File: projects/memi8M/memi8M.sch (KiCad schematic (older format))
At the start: 38 parts, among them J1 Conn_01x06, J2 Conn_01x02, J3 Conn_01x03, J4 Conn_01x06, SW1 SW_DIP_x05, U1 74HC595N, U10 74LS166N, U11 SST39VF1681_1682, U12 74LVC4245, U2 74HC595N, U3 74HC595N, U4 74HC595N, U5 SFC_MaskRom_32pin_SOCKET, U6 74LVC245, U7 74LVC245, U8 74LVC245, U9 LD1117S33TR

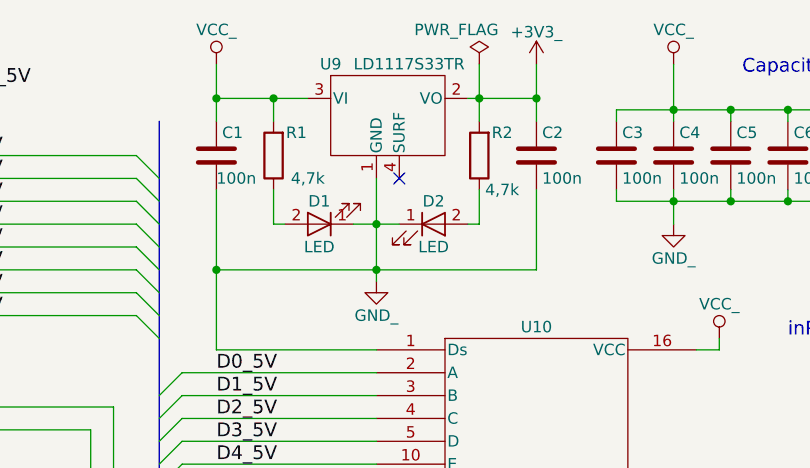
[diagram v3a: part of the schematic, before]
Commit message: Some module renamed for better overall accessibility. BOM updated. .net created. Modules associated to .net and schema.
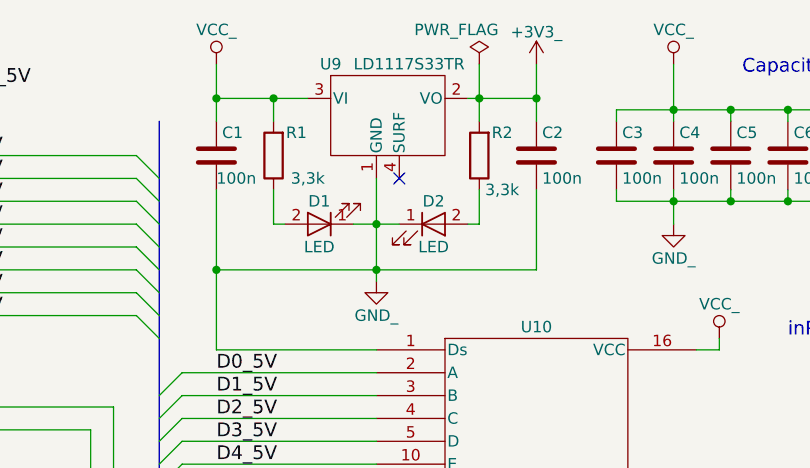
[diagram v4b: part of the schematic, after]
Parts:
- C1, C10, C11, C12, C13, C2, C3, C4, C5, C6, C7, C8, C9, D1, D2, R3, R4, R5, R6: footprint (none) -> alf64_mods:0805
- J1, J4: footprint PINHEAD1x6 -> alf64_mods:PINHEAD1x6
- J2: footprint PINHEAD1x2 -> alf64_mods:PINHEAD1x2
- J3: footprint PINHEAD1x3 -> alf64_mods:PINHEAD1x3
- R1, R2: value 4,7k -> 3,3k; footprint (none) -> alf64_mods:0805
- SW1: footprint (none) -> alf64_mods:SW_DIP_x05
- U1, U2, U3, U4: footprint SO16 -> alf64_mods:SO16
- U10: footprint (none) -> alf64_mods:SO16
- U11: footprint (none) -> alf64_mods:GOTRONIK_ADAP_TSOP48
- U12: footprint (none) -> alf64_mods:SO24
- U5: footprint PDIP32 -> alf64_mods:PDIP32
- U6, U7, U8: footprint 74LVC245_SO20 -> alf64_mods:SO20
- U9: footprint (none) -> alf64_mods:SOT223
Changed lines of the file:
@@
 F 0 "U1" H 2050 1900 50  0000 C CNN
 F 1 "74HC595N" H 1900 700 50  0000 C CNN
-F 2 "SO16" H 1900 1300 50  0001 C CNN
+F 2 "alf64_mods:SO16" H 1900 1300 50  0001 C CNN
 F 3 "" H 1900 1300 50  0001 C CNN
 	1    1900 1300
@@
 F 0 "U2" H 2050 3300 50  0000 C CNN
 F 1 "74HC595N" H 1900 2100 50  0000 C CNN
-F 2 "SO16" H 1900 2700 50  0001 C CNN
+F 2 "alf64_mods:SO16" H 1900 2700 50  0001 C CNN
 F 3 "" H 1900 2700 50  0001 C CNN
 	1    1900 2700
@@
 F 0 "U3" H 2050 4700 50  0000 C CNN
 F 1 "74HC595N" H 1900 3500 50  0000 C CNN
-F 2 "SO16" H 1900 4100 50  0001 C CNN
+F 2 "alf64_mods:SO16" H 1900 4100 50  0001 C CNN
 F 3 "" H 1900 4100 50  0001 C CNN
 	1    1900 4100
@@
 F 0 "U6" H 4700 4600 60  0000 C CNN
 F 1 "74LVC245" H 4700 3400 60  0000 C CNN
-F 2 "74LVC245_SO20" H 4700 3300 60  0001 C CNN
+F 2 "alf64_mods:SO20" H 4700 3300 60  0001 C CNN
 F 3 "" H 4700 4000 60  0001 C CNN
 	1    4700 4000
@@
 F 0 "U7" H 4700 6050 60  0000 C CNN
 F 1 "74LVC245" H 4700 4850 60  0000 C CNN
-F 2 "74LVC245_SO20" H 4700 4750 60  0001 C CNN
+F 2 "alf64_mods:SO20" H 4700 4750 60  0001 C CNN
 F 3 "" H 4700 5450 60  0001 C CNN
 	1    4700 5450
@@
 F 0 "U8" H 4700 7500 60  0000 C CNN
 F 1 "74LVC245" H 4700 6300 60  0000 C CNN
-F 2 "74LVC245_SO20" H 4700 6200 60  0001 C CNN
+F 2 "alf64_mods:SO20" H 4700 6200 60  0001 C CNN
 F 3 "" H 4700 6900 60  0001 C CNN
 	1    4700 6900
@@
 F 0 "U5" H 4750 2450 60  0000 C CNN
 F 1 "SFC_MaskRom_32pin_SOCKET" H 4700 200 60  0000 C CNN
-F 2 "PDIP32" H 4750 2450 60  0001 C CNN
+F 2 "alf64_mods:PDIP32" H 4750 2450 60  0001 C CNN
 F 3 "" H 4750 2450 60  0001 C CNN
 	1    4750 1550
@@
 F 0 "U11" H 7250 5400 60  0000 C CNN
 F 1 "SST39VF1681_1682" H 7250 3150 60  0000 C CNN
-F 2 "" H 7250 5400 60  0001 C CNN
+F 2 "alf64_mods:GOTRONIK_ADAP_TSOP48" H 7250 5400 60  0001 C CNN
 F 3 "" H 7250 5400 60  0001 C CNN
 	1    7250 4600
@@
 F 0 "U4" H 2050 6100 50  0000 C CNN
 F 1 "74HC595N" H 1900 4900 50  0000 C CNN
-F 2 "SO16" H 1900 5500 50  0001 C CNN
+F 2 "alf64_mods:SO16" H 1900 5500 50  0001 C CNN
 F 3 "" H 1900 5500 50  0001 C CNN
 	1    1900 5500
@@
 F 0 "U12" H 9000 5000 60  0000 C CNN
 F 1 "74LVC4245" H 9000 3600 60  0000 C CNN
-F 2 "" H 9000 4400 60  0001 C CNN
+F 2 "alf64_mods:SO24" H 9000 4400 60  0001 C CNN
 F 3 "" H 9000 4400 60  0001 C CNN
 	1    9000 4400
@@
 F 0 "U10" H 8100 3400 50  0000 C CNN
 F 1 "74LS166N" H 8100 1900 50  0000 C CNN
-F 2 "" H 8100 2650 50  0001 C CNN
+F 2 "alf64_mods:SO16" H 8100 2650 50  0001 C CNN
 F 3 "" H 8100 2650 50  0001 C CNN
 	1    8100 2650
@@
 F 0 "C1" H 6725 1250 50  0000 L CNN
 F 1 "100n" H 6700 1050 50  0000 L CNN
-F 2 "" H 6738 1000 50  0001 C CNN
+F 2 "alf64_mods:0805" H 6738 1000 50  0001 C CNN
 F 3 "" H 6700 1150 50  0001 C CNN
 	1    6700 1150
@@
 F 0 "C2" H 8125 1250 50  0000 L CNN
 F 1 "100n" H 8125 1050 50  0000 L CNN
-F 2 "" H 8138 1000 50  0001 C CNN
+F 2 "alf64_mods:0805" H 8138 1000 50  0001 C CNN
 F 3 "" H 8100 1150 50  0001 C CNN
 	1    8100 1150
@@
 F 0 "R3" V 10750 1950 50  0000 C CNN
 F 1 "100" V 10800 2150 50  0000 C CNN
-F 2 "" V 10730 2150 50  0001 C CNN
+F 2 "alf64_mods:0805" V 10730 2150 50  0001 C CNN
 F 3 "" H 10800 2150 50  0001 C CNN
 	1    10800 2150
@@
 F 0 "R5" V 10750 2150 50  0000 C CNN
 F 1 "100" V 10800 2350 50  0000 C CNN
-F 2 "" V 10730 2350 50  0001 C CNN
+F 2 "alf64_mods:0805" V 10730 2350 50  0001 C CNN
 F 3 "" H 10800 2350 50  0001 C CNN
 	1    10800 2350
@@
 F 0 "R4" V 10750 2050 50  0000 C CNN
 F 1 "100" V 10800 2250 50  0000 C CNN
-F 2 "" V 10730 2250 50  0001 C CNN
+F 2 "alf64_mods:0805" V 10730 2250 50  0001 C CNN
 F 3 "" H 10800 2250 50  0001 C CNN
 	1    10800 2250
@@
 F 0 "J1" H 800 7050 50  0000 C CNN
 F 1 "Conn_01x06" H 800 6350 50  0000 C CNN
-F 2 "PINHEAD1x6" H 800 6750 50  0001 C CNN
+F 2 "alf64_mods:PINHEAD1x6" H 800 6750 50  0001 C CNN
 F 3 "" H 800 6750 50  0001 C CNN
 	1    800  6750
@@
 F 0 "J2" H 800 7550 50  0000 C CNN
 F 1 "Conn_01x02" H 800 7250 50  0000 C CNN
-F 2 "PINHEAD1x2" H 800 7450 50  0001 C CNN
+F 2 "alf64_mods:PINHEAD1x2" H 800 7450 50  0001 C CNN
 F 3 "" H 800 7450 50  0001 C CNN
 	1    800  7450
@@
 F 0 "J3" H 2800 6700 50  0000 C CNN
 F 1 "Conn_01x03" H 2800 6300 50  0000 C CNN
-F 2 "PINHEAD1x3" H 2800 6500 50  0001 C CNN
+F 2 "alf64_mods:PINHEAD1x3" H 2800 6500 50  0001 C CNN
 F 3 "" H 2800 6500 50  0001 C CNN
 	1    2800 6500
@@
 F 0 "R6" V 10750 2250 50  0000 C CNN
 F 1 "100" V 10800 2450 50  0000 C CNN
-F 2 "" V 10730 2450 50  0001 C CNN
+F 2 "alf64_mods:0805" V 10730 2450 50  0001 C CNN
 F 3 "" H 10800 2450 50  0001 C CNN
 	1    10800 2450
@@
 F 0 "C8" H 9725 1250 50  0000 L CNN
 F 1 "100n" H 9725 1050 50  0000 L CNN
-F 2 "" H 9738 1000 50  0001 C CNN
+F 2 "alf64_mods:0805" H 9738 1000 50  0001 C CNN
 F 3 "" H 9700 1150 50  0001 C CNN
 	1    9700 1150
@@
 F 0 "C10" H 10275 1250 50  0000 L CNN
 F 1 "100n" H 10275 1050 50  0000 L CNN
-F 2 "" H 10288 1000 50  0001 C CNN
+F 2 "alf64_mods:0805" H 10288 1000 50  0001 C CNN
 F 3 "" H 10250 1150 50  0001 C CNN
 	1    10250 1150
@@
 F 0 "C11" H 10525 1250 50  0000 L CNN
 F 1 "100n" H 10525 1050 50  0000 L CNN
-F 2 "" H 10538 1000 50  0001 C CNN
+F 2 "alf64_mods:0805" H 10538 1000 50  0001 C CNN
 F 3 "" H 10500 1150 50  0001 C CNN
 	1    10500 1150
@@
 F 0 "C12" H 10775 1250 50  0000 L CNN
 F 1 "100n" H 10775 1050 50  0000 L CNN
-F 2 "" H 10788 1000 50  0001 C CNN
+F 2 "alf64_mods:0805" H 10788 1000 50  0001 C CNN
 F 3 "" H 10750 1150 50  0001 C CNN
 	1    10750 1150
@@
 F 0 "C13" H 11025 1250 50  0000 L CNN
 F 1 "100n" H 11025 1050 50  0000 L CNN
-F 2 "" H 11038 1000 50  0001 C CNN
+F 2 "alf64_mods:0805" H 11038 1000 50  0001 C CNN
 F 3 "" H 11000 1150 50  0001 C CNN
 	1    11000 1150
@@
 F 0 "C3" H 8475 1250 50  0000 L CNN
 F 1 "100n" H 8475 1050 50  0000 L CNN
-F 2 "" H 8488 1000 50  0001 C CNN
+F 2 "alf64_mods:0805" H 8488 1000 50  0001 C CNN
 F 3 "" H 8450 1150 50  0001 C CNN
 	1    8450 1150
@@
 F 0 "C4" H 8725 1250 50  0000 L CNN
 F 1 "100n" H 8725 1050 50  0000 L CNN
-F 2 "" H 8738 1000 50  0001 C CNN
+F 2 "alf64_mods:0805" H 8738 1000 50  0001 C CNN
 F 3 "" H 8700 1150 50  0001 C CNN
 	1    8700 1150
@@
 F 0 "C5" H 8975 1250 50  0000 L CNN
 F 1 "100n" H 8975 1050 50  0000 L CNN
-F 2 "" H 8988 1000 50  0001 C CNN
+F 2 "alf64_mods:0805" H 8988 1000 50  0001 C CNN
 F 3 "" H 8950 1150 50  0001 C CNN
 	1    8950 1150
@@
 F 0 "C6" H 9225 1250 50  0000 L CNN
 F 1 "100n" H 9225 1050 50  0000 L CNN
-F 2 "" H 9238 1000 50  0001 C CNN
+F 2 "alf64_mods:0805" H 9238 1000 50  0001 C CNN
 F 3 "" H 9200 1150 50  0001 C CNN
 	1    9200 1150
@@
 F 0 "C7" H 9475 1250 50  0000 L CNN
 F 1 "100n" H 9475 1050 50  0000 L CNN
-F 2 "" H 9488 1000 50  0001 C CNN
+F 2 "alf64_mods:0805" H 9488 1000 50  0001 C CNN
 F 3 "" H 9450 1150 50  0001 C CNN
 	1    9450 1150
@@
 F 0 "C9" H 10025 1250 50  0000 L CNN
 F 1 "100n" H 10025 1050 50  0000 L CNN
-F 2 "" H 10038 1000 50  0001 C CNN
+F 2 "alf64_mods:0805" H 10038 1000 50  0001 C CNN
 F 3 "" H 10000 1150 50  0001 C CNN
 	1    10000 1150
@@
 F 0 "SW1" H 10100 2700 50  0000 C CNN
 F 1 "SW_DIP_x05" H 10100 2000 50  0000 C CNN
-F 2 "" H 10100 2350 50  0001 C CNN
+F 2 "alf64_mods:SW_DIP_x05" H 10100 2350 50  0001 C CNN
 F 3 "" H 10100 2350 50  0001 C CNN
 	1    10100 2350
@@
 F 0 "J4" H 2800 7550 50  0000 C CNN
 F 1 "Conn_01x06" H 2800 6850 50  0000 C CNN
-F 2 "PINHEAD1x6" H 2800 7250 50  0001 C CNN
+F 2 "alf64_mods:PINHEAD1x6" H 2800 7250 50  0001 C CNN
 F 3 "" H 2800 7250 50  0001 C CNN
 	1    2800 7250
@@
 P 6950 1150
 F 0 "R1" H 6850 1050 50  0000 C CNN
-F 1 "4,7k" H 6800 1250 50  0000 C CNN
-F 2 "" V 6880 1150 50  0001 C CNN
+F 1 "3,3k" H 6800 1250 50  0000 C CNN
+F 2 "alf64_mods:0805" V 6880 1150 50  0001 C CNN
 F 3 "" H 6950 1150 50  0001 C CNN
 	1    6950 1150
@@
 P 7850 1150
 F 0 "R2" H 7750 1050 50  0000 C CNN
-F 1 "4,7k" H 7750 1300 50  0000 C CNN
-F 2 "" V 7780 1150 50  0001 C CNN
+F 1 "3,3k" H 7750 1300 50  0000 C CNN
+F 2 "alf64_mods:0805" V 7780 1150 50  0001 C CNN
 F 3 "" H 7850 1150 50  0001 C CNN
 	1    7850 1150
@@
 F 0 "D1" H 7150 1350 50  0000 C CNN
 F 1 "LED" H 7150 1550 50  0000 C CNN
-F 2 "" H 7150 1450 50  0001 C CNN
+F 2 "alf64_mods:0805" H 7150 1450 50  0001 C CNN
 F 3 "" H 7150 1450 50  0001 C CNN
 	1    7150 1450
@@
 F 0 "D2" H 7650 1550 50  0000 C CNN
 F 1 "LED" H 7650 1350 50  0000 C CNN
-F 2 "" H 7650 1450 50  0001 C CNN
+F 2 "alf64_mods:0805" H 7650 1450 50  0001 C CNN
 F 3 "" H 7650 1450 50  0001 C CNN
 	1    7650 1450
@@
 F 0 "U9" H 7200 1150 50  0000 C CNN
 F 1 "LD1117S33TR" H 7300 1150 50  0000 L CNN
-F 2 "" H 6600 1150 50  0001 C CNN
+F 2 "alf64_mods:SOT223" H 6600 1150 50  0001 C CNN
 F 3 "" H 6700 750 50  0001 C CNN
 	1    7450 950
